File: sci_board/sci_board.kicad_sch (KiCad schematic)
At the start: 0 parts

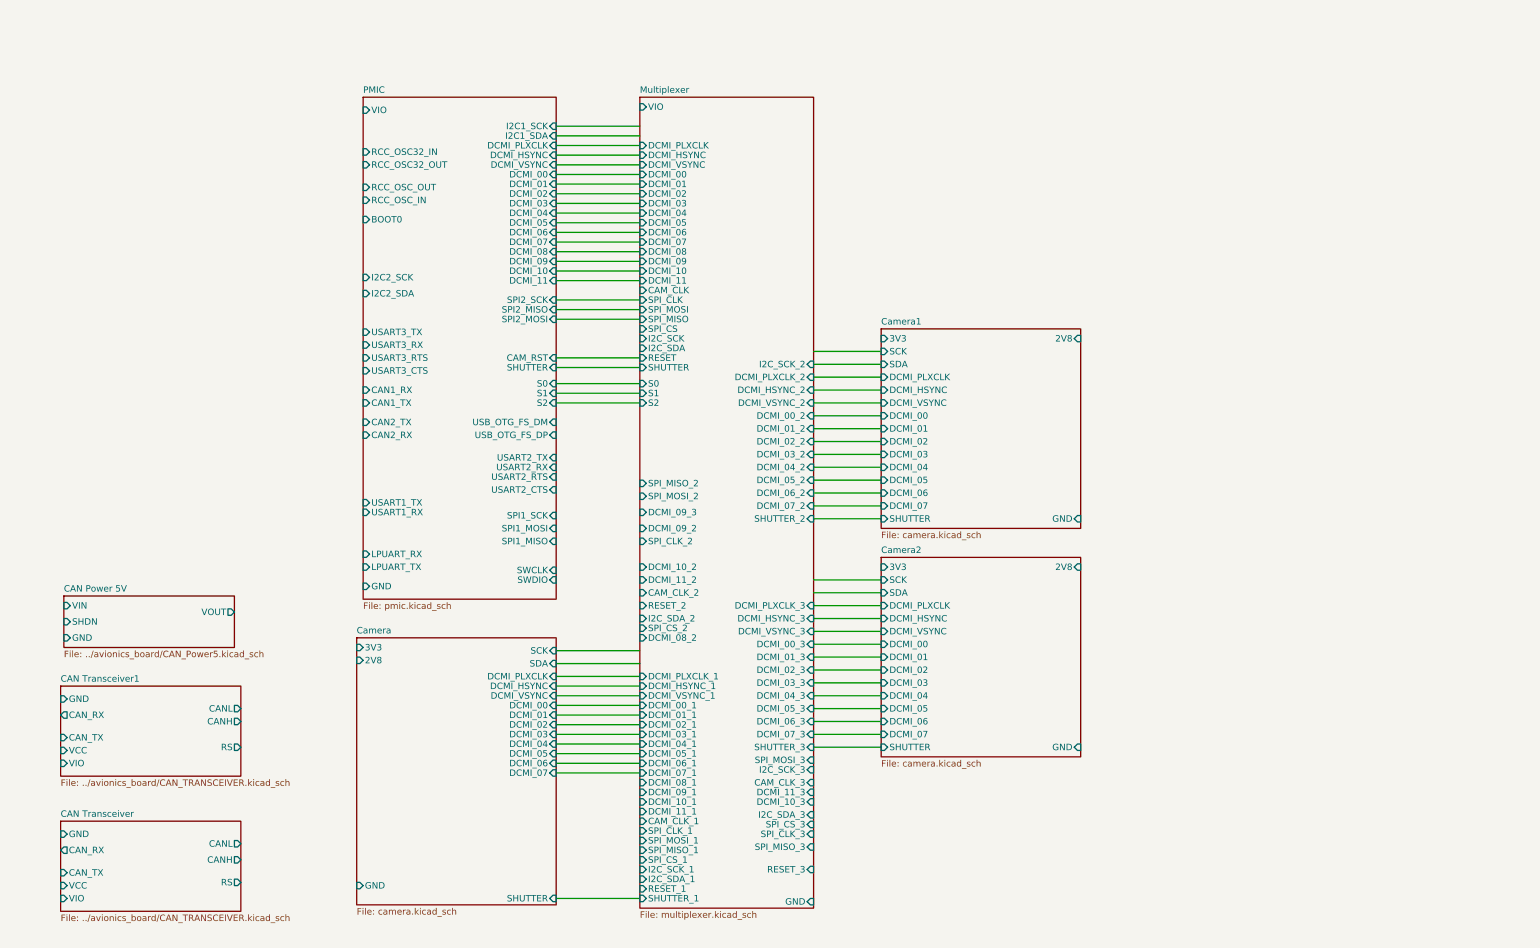
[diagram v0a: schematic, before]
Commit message: draft of science board: add USB and thermal imager, sort out power switches for cameras
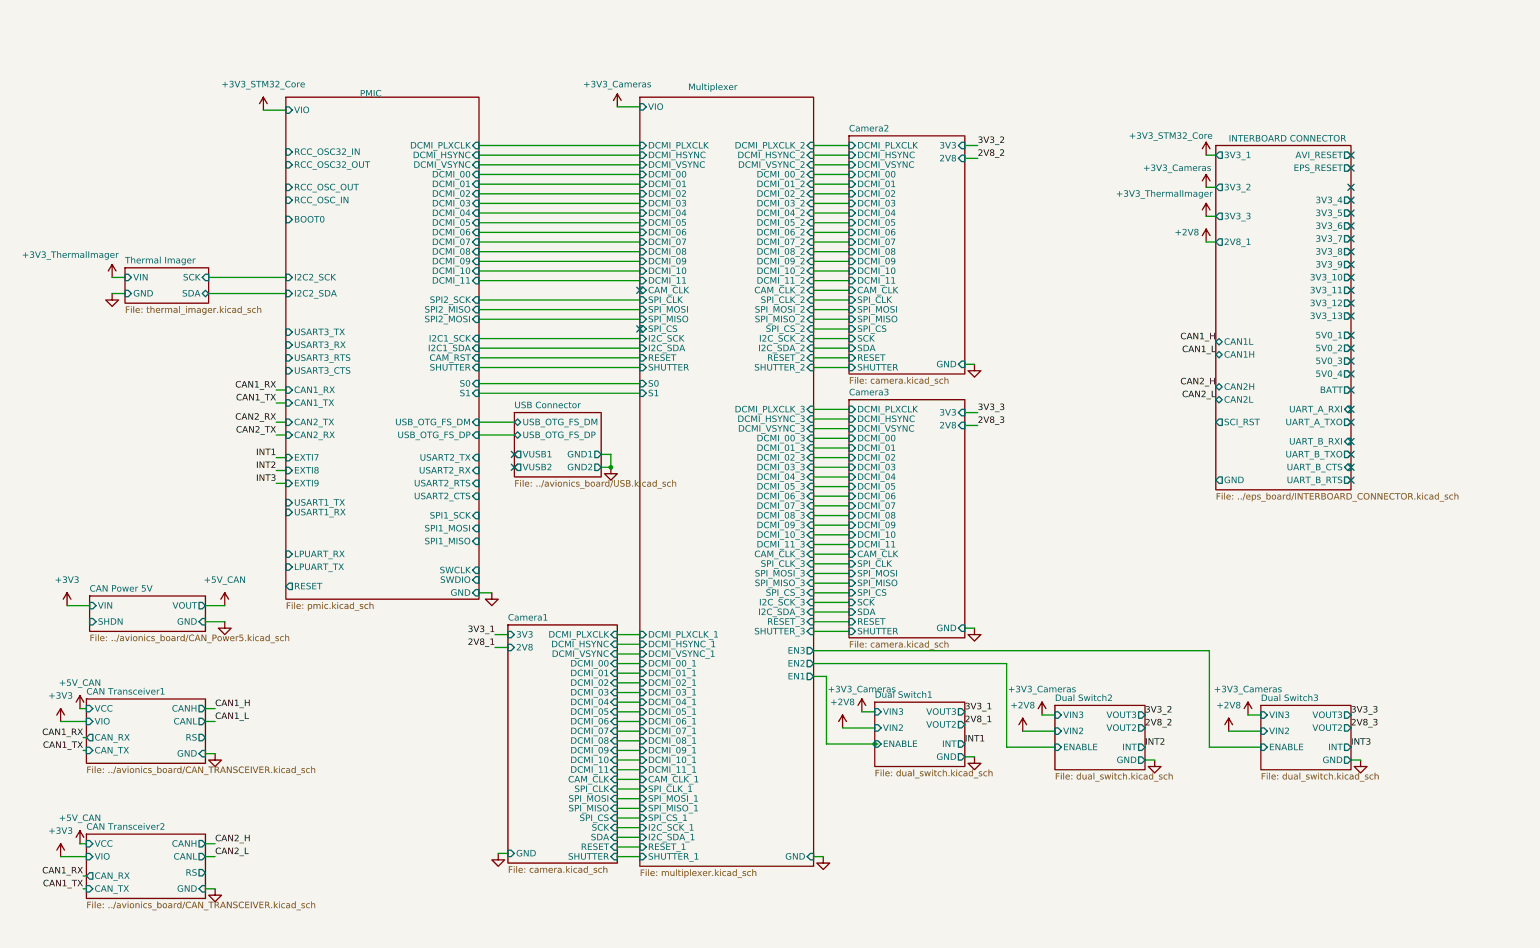
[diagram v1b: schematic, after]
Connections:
- no-connect marks 0 -> 28
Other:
- sheet CAN Transceiver renamed CAN Transceiver2
- removed sheet Camera
- added sheet Camera3 (camera.kicad_sch)
- added sheet Dual Switch1 (dual_switch.kicad_sch)
- added sheet Dual Switch2 (dual_switch.kicad_sch)
- added sheet Dual Switch3 (dual_switch.kicad_sch)
- added sheet INTERBOARD CONNECTOR (../eps_board/INTERBOARD_CONNECTOR.kicad_sch)
- added sheet Thermal Imager (thermal_imager.kicad_sch)
- added sheet USB Connector (../avionics_board/USB.kicad_sch)
- sheet Camera1 ports: added CAM_CLK, DCMI_08, DCMI_09, DCMI_10, DCMI_11, RESET, SPI_CLK, SPI_CS, SPI_MISO, SPI_MOSI; removed none
- sheet Camera2 ports: added CAM_CLK, DCMI_08, DCMI_09, DCMI_10, DCMI_11, RESET, SPI_CLK, SPI_CS, SPI_MISO, SPI_MOSI; removed none
- sheet Multiplexer ports: added DCMI_08_3, EN1, EN2, EN3; removed S2
- sheet PMIC ports: added EXTI7, EXTI8, EXTI9, RESET; removed S2

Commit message: SCI board: add flash and mram; decorate PMC with boot, reset, etc
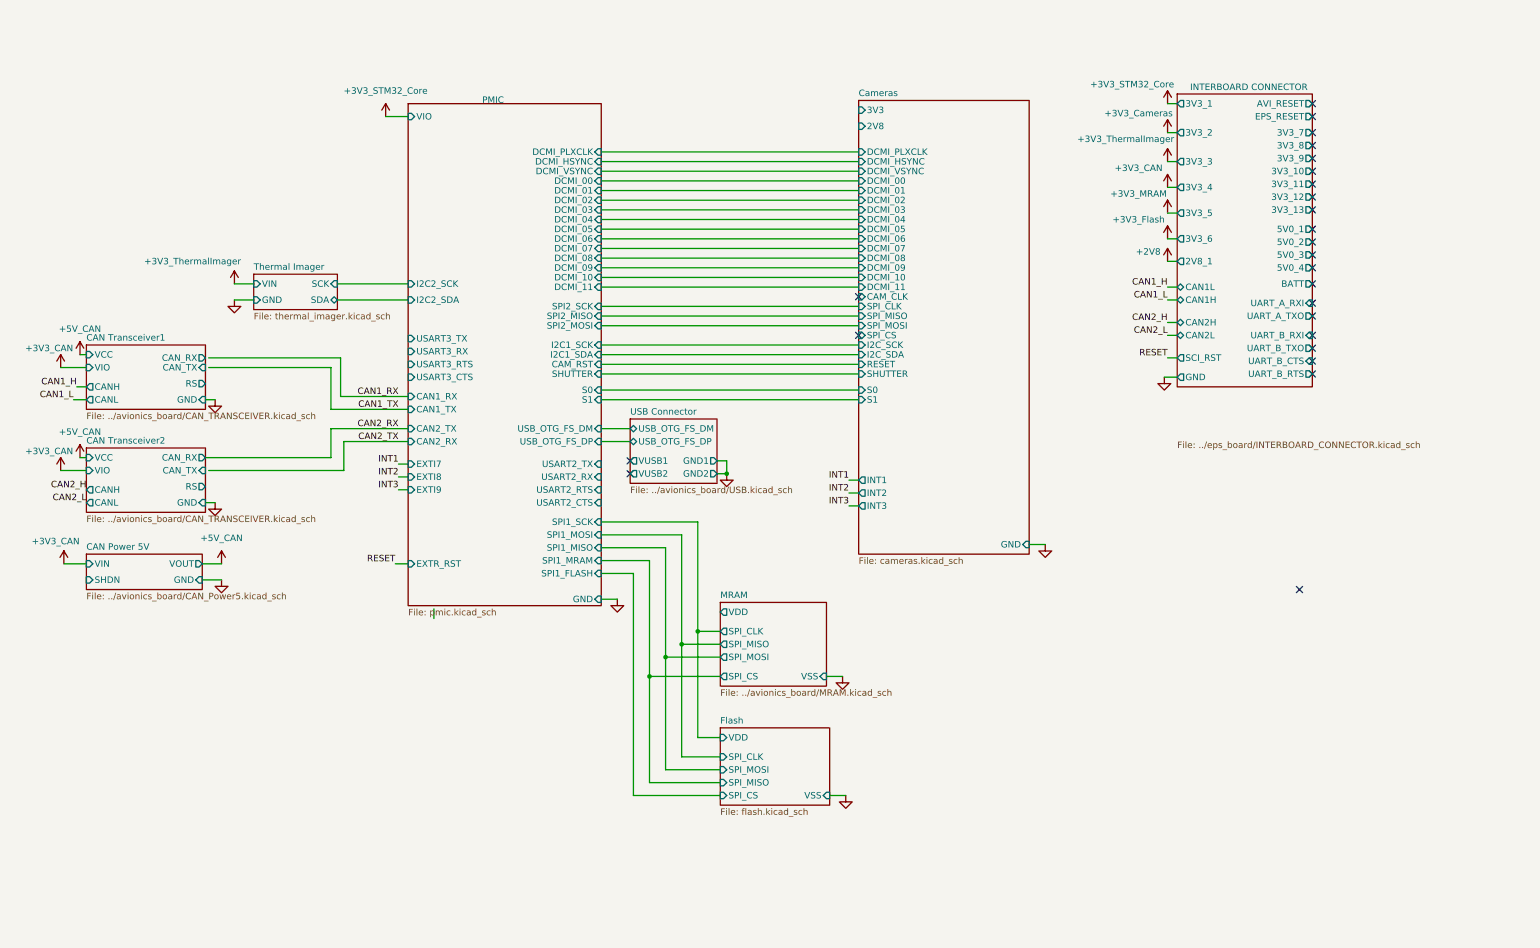
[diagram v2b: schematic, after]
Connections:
- no-connect marks 28 -> 25
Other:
- removed sheet Camera1
- removed sheet Camera2
- removed sheet Camera3
- removed sheet Dual Switch1
- removed sheet Dual Switch2
- removed sheet Dual Switch3
- removed sheet Multiplexer
- added sheet Cameras (cameras.kicad_sch)
- added sheet Flash (flash.kicad_sch)
- added sheet MRAM (../avionics_board/MRAM.kicad_sch)
- sheet PMIC ports: added EXTR_RST, SPI1_FLASH, SPI1_MRAM; removed BOOT0, LPUART_RX, LPUART_TX, RCC_OSC32_IN, RCC_OSC32_OUT, RCC_OSC_IN, RCC_OSC_OUT, RESET, SWCLK, SWDIO, USART1_RX, USART1_TX

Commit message: start SCI pcb
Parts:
- added H1, H2, H3, H4: MountingHole_Pad, Project:MountingHole_4.3mm_M4_Pad_Via_Custom, symbol Mechanical:MountingHole_Pad
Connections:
- net GND: now also H1.1, H2.1, H3.1, H4.1
- no-connect marks 25 -> 32
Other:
- sheet PMIC ports: added CAN_RS; removed none

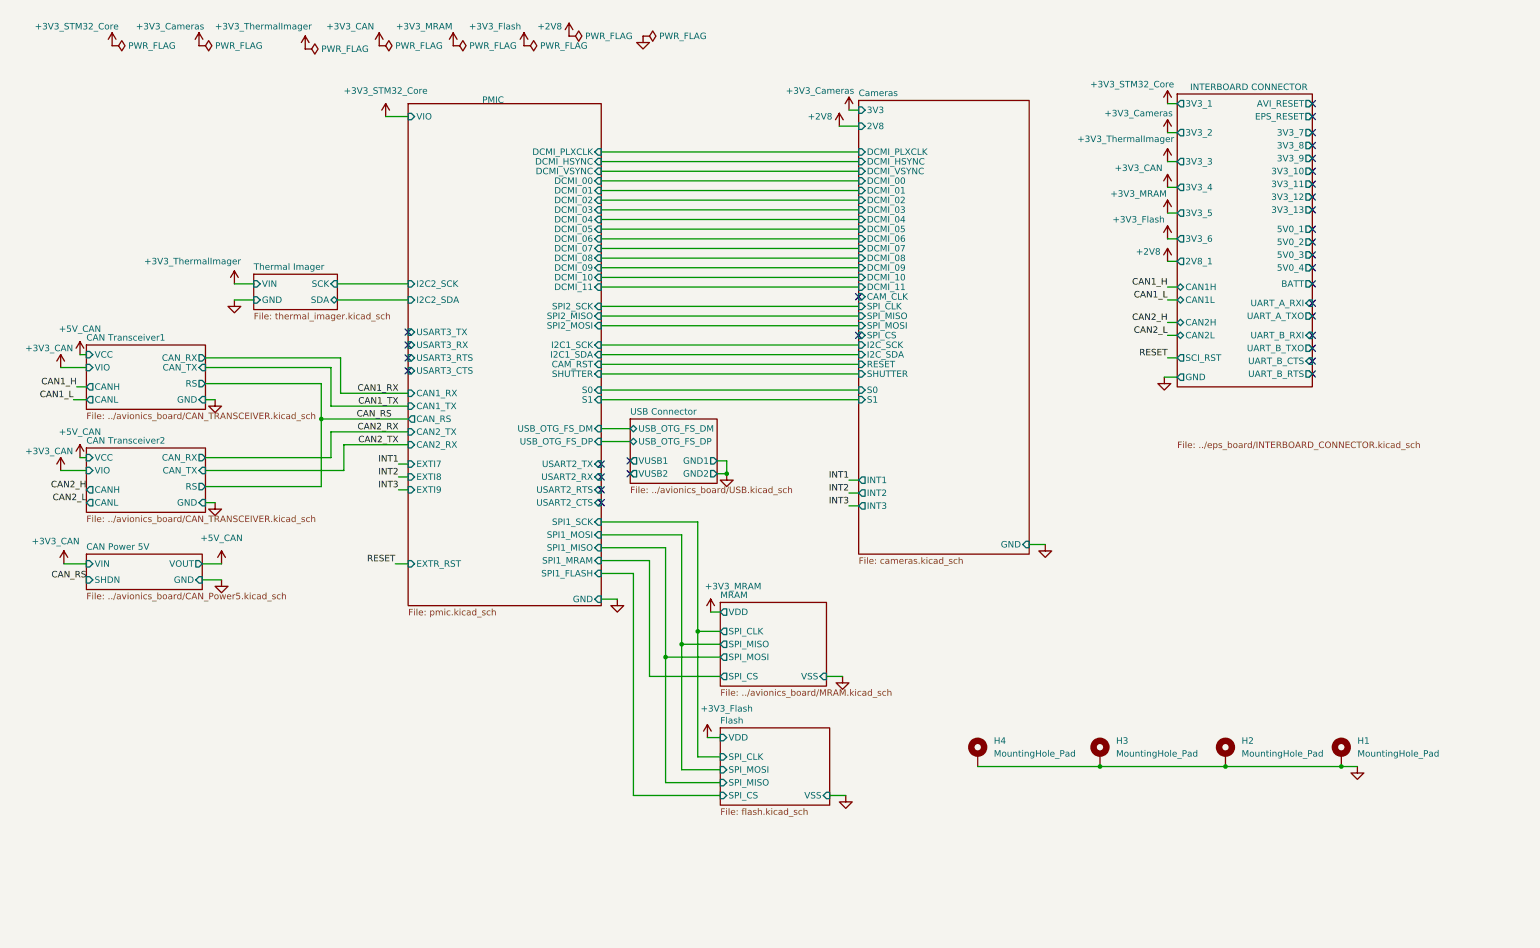
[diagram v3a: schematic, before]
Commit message: begin to update the pcb
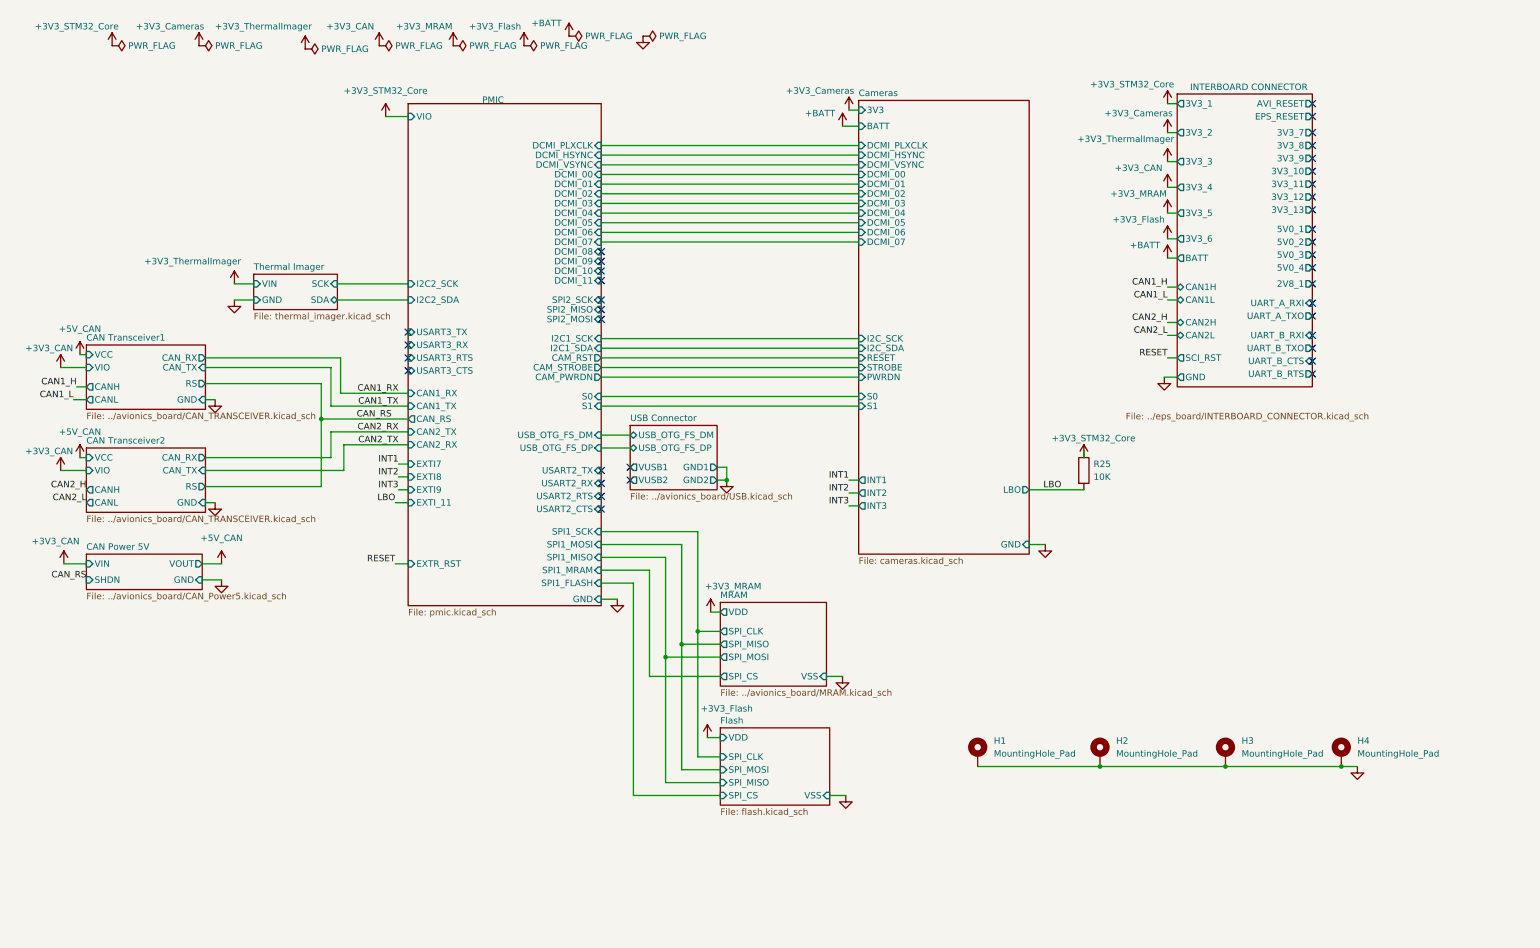
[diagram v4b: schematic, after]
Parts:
- added R25: 10K, Resistor_SMD:R_0603_1608Metric_Pad0.98x0.95mm_HandSolder, symbol Device:R
- renumbered H4 to H1, H3 to H2, H2 to H3, H1 to H4
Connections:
- net +3V3_STM32_Core: now also R25.1
- new net LBO: R25.2
- no-connect marks 32 -> 37
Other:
- sheet Cameras ports: added BATT, LBO, PWRDN, STROBE; removed 2V8, CAM_CLK, DCMI_08, DCMI_09, DCMI_10, DCMI_11, SHUTTER, SPI_CLK, SPI_CS, SPI_MISO, SPI_MOSI
- sheet PMIC ports: added CAM_PWRDN, CAM_STROBE, EXTI_11; removed SHUTTER

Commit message: continue layout
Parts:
- renumbered R25 to R1
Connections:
- no-connect marks 37 -> 36
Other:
- sheet Cameras ports: added 5V0; removed none
